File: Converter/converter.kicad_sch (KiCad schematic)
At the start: 39 parts, among them IC1 NCP5109ADR2G, IC2 NCP5109ADR2G, J3 XT30, J4 XT30

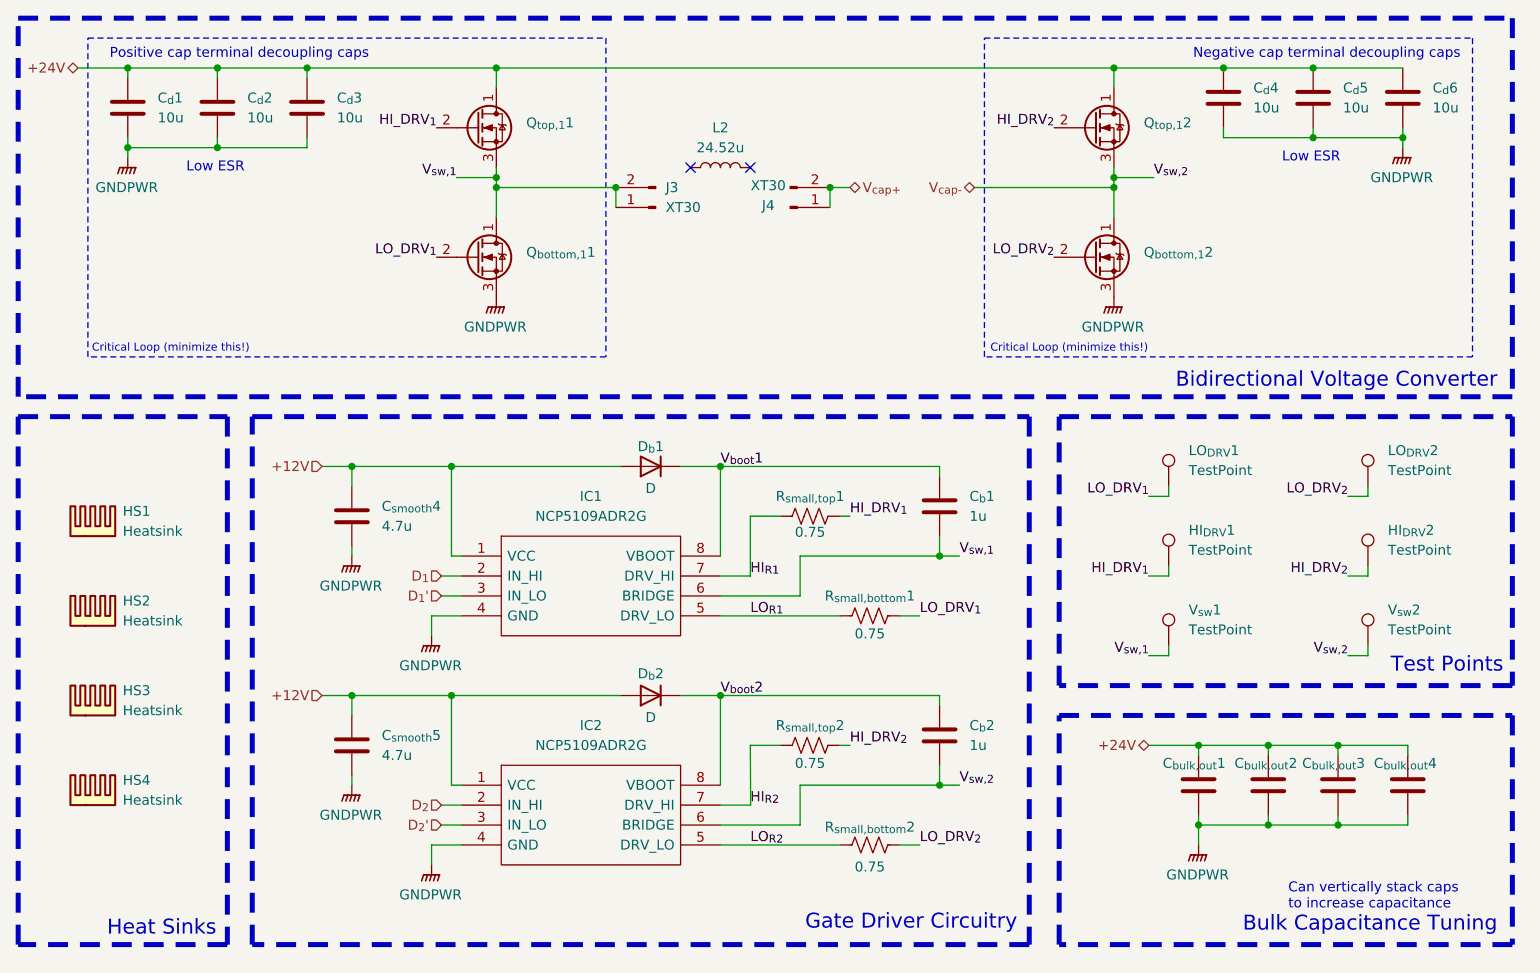
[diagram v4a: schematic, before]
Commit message: cleaned up PCB after meeting with BBJ
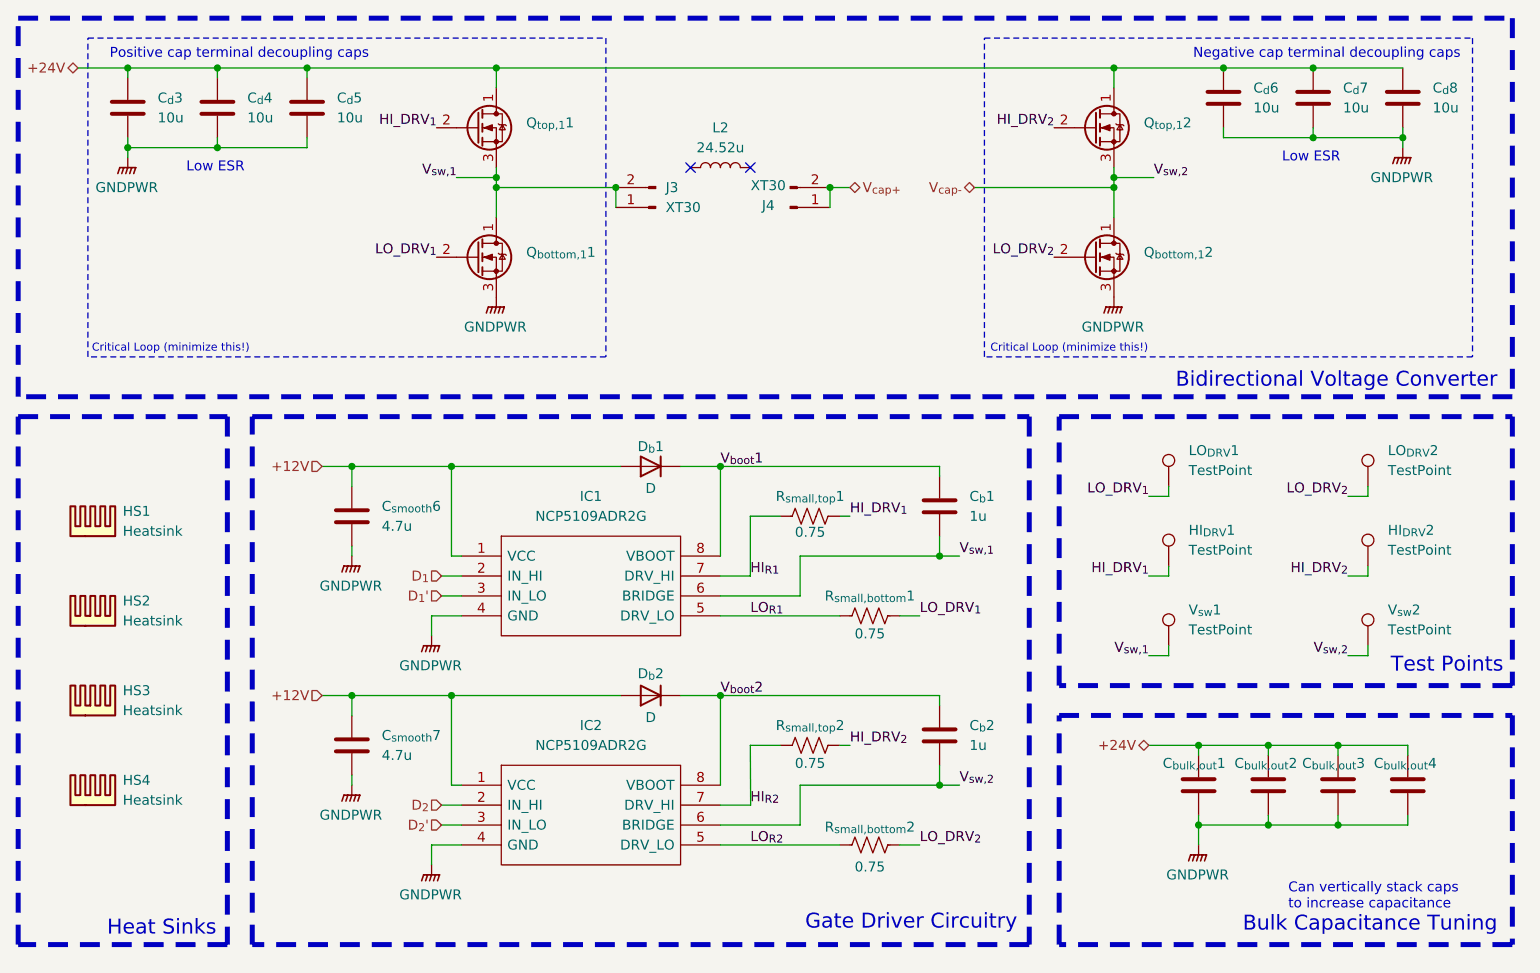
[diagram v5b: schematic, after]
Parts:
- renumbered C_{d}1 to C_{d}3, C_{d}2 to C_{d}4, C_{d}3 to C_{d}5, C_{d}4 to C_{d}6, C_{d}5 to C_{d}7, C_{d}6 to C_{d}8, C_{smooth}4 to C_{smooth}6, C_{smooth}5 to C_{smooth}7
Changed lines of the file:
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@@
 		(dnp no)
 		(fields_autoplaced yes)
-		(property "Reference" "#PWR025"
+		(property "Reference" "#PWR029"
 			(at 85.09 143.51 0)
 			(effects
@@
 			(project "Supercap"
 				(path "/98ee8313-37ab-4329-91ab-b5710476f82f/66de8ce3-68f9-4d35-858c-1420192a373c"
-					(reference "#PWR025")
+					(reference "#PWR029")
 					(unit 1)
 				)
@@
 		(dnp no)
 		(fields_autoplaced yes)
-		(property "Reference" "C_{smooth}5"
+		(property "Reference" "C_{smooth}7"
 			(at 88.9 132.0799 0)
 			(effects
@@
 			(project "Supercap"
 				(path "/98ee8313-37ab-4329-91ab-b5710476f82f/66de8ce3-68f9-4d35-858c-1420192a373c"
-					(reference "C_{smooth}5")
+					(reference "C_{smooth}7")
 					(unit 1)
 				)
@@
 		(on_board yes)
 		(dnp no)
-		(property "Reference" "C_{d}3"
+		(property "Reference" "C_{d}5"
 			(at 83.185 50.7999 0)
 			(effects
@@
 			(project "Supercap"
 				(path "/98ee8313-37ab-4329-91ab-b5710476f82f/66de8ce3-68f9-4d35-858c-1420192a373c"
-					(reference "C_{d}3")
+					(reference "C_{d}5")
 					(unit 1)
 				)
@@
 		(dnp no)
 		(fields_autoplaced yes)
-		(property "Reference" "#PWR023"
+		(property "Reference" "#PWR027"
 			(at 56.515 63.5 0)
 			(effects
@@
 			(project "Supercap"
 				(path "/98ee8313-37ab-4329-91ab-b5710476f82f/66de8ce3-68f9-4d35-858c-1420192a373c"
-					(reference "#PWR023")
+					(reference "#PWR027")
 					(unit 1)
 				)
@@
 		(dnp no)
 		(fields_autoplaced yes)
-		(property "Reference" "#PWR030"
+		(property "Reference" "#PWR034"
 			(at 193.04 151.13 0)
 			(effects
@@
 			(project "Supercap"
 				(path "/98ee8313-37ab-4329-91ab-b5710476f82f/66de8ce3-68f9-4d35-858c-1420192a373c"
-					(reference "#PWR030")
+					(reference "#PWR034")
 					(unit 1)
 				)
@@
 		(on_board yes)
 		(dnp no)
-		(property "Reference" "C_{d}4"
+		(property "Reference" "C_{d}6"
 			(at 200.025 49.5299 0)
 			(effects
@@
 			(project "Supercap"
 				(path "/98ee8313-37ab-4329-91ab-b5710476f82f/66de8ce3-68f9-4d35-858c-1420192a373c"
-					(reference "C_{d}4")
+					(reference "C_{d}6")
 					(unit 1)
 				)
@@
 		(dnp no)
 		(fields_autoplaced yes)
-		(property "Reference" "#PWR031"
+		(property "Reference" "#PWR035"
 			(at 219.075 62.23 0)
 			(effects
@@
 			(project "Supercap"
 				(path "/98ee8313-37ab-4329-91ab-b5710476f82f/66de8ce3-68f9-4d35-858c-1420192a373c"
-					(reference "#PWR031")
+					(reference "#PWR035")
 					(unit 1)
 				)
@@
 		(dnp no)
 		(fields_autoplaced yes)
-		(property "Reference" "#PWR029"
+		(property "Reference" "#PWR033"
 			(at 182.245 81.28 0)
 			(effects
@@
 			(project "Supercap"
 				(path "/98ee8313-37ab-4329-91ab-b5710476f82f/66de8ce3-68f9-4d35-858c-1420192a373c"
-					(reference "#PWR029")
+					(reference "#PWR033")
 					(unit 1)
 				)
@@
 		(dnp no)
 		(fields_autoplaced yes)
-		(property "Reference" "#PWR027"
+		(property "Reference" "#PWR031"
 			(at 95.25 153.67 0)
 			(effects
@@
 			(project "Supercap"
 				(path "/98ee8313-37ab-4329-91ab-b5710476f82f/66de8ce3-68f9-4d35-858c-1420192a373c"
-					(reference "#PWR027")
+					(reference "#PWR031")
 					(unit 1)
 				)
@@
 		(dnp no)
 		(fields_autoplaced yes)
-		(property "Reference" "C_{smooth}4"
+		(property "Reference" "C_{smooth}6"
 			(at 88.9 102.8699 0)
 			(effects
@@
 			(project "Supercap"
 				(path "/98ee8313-37ab-4329-91ab-b5710476f82f/66de8ce3-68f9-4d35-858c-1420192a373c"
-					(reference "C_{smooth}4")
+					(reference "C_{smooth}6")
 					(unit 1)
 				)
@@
 		(on_board yes)
 		(dnp no)
-		(property "Reference" "C_{d}1"
+		(property "Reference" "C_{d}3"
 			(at 60.325 50.7999 0)
 			(effects
@@
 			(project "Supercap"
 				(path "/98ee8313-37ab-4329-91ab-b5710476f82f/66de8ce3-68f9-4d35-858c-1420192a373c"
-					(reference "C_{d}1")
+					(reference "C_{d}3")
 					(unit 1)
 				)
@@
 		(on_board yes)
 		(dnp no)
-		(property "Reference" "C_{d}2"
+		(property "Reference" "C_{d}4"
 			(at 71.755 50.7999 0)
 			(effects
@@
 			(project "Supercap"
 				(path "/98ee8313-37ab-4329-91ab-b5710476f82f/66de8ce3-68f9-4d35-858c-1420192a373c"
-					(reference "C_{d}2")
+					(reference "C_{d}4")
 					(unit 1)
 				)
@@
 		(on_board yes)
 		(dnp no)
-		(property "Reference" "C_{d}6"
+		(property "Reference" "C_{d}8"
 			(at 222.885 49.5299 0)
 			(effects
@@
 			(project "Supercap"
 				(path "/98ee8313-37ab-4329-91ab-b5710476f82f/66de8ce3-68f9-4d35-858c-1420192a373c"
-					(reference "C_{d}6")
+					(reference "C_{d}8")
 					(unit 1)
 				)
@@
 		(on_board yes)
 		(dnp no)
-		(property "Reference" "C_{d}5"
+		(property "Reference" "C_{d}7"
 			(at 211.455 49.5299 0)
 			(effects
@@
 			(project "Supercap"
 				(path "/98ee8313-37ab-4329-91ab-b5710476f82f/66de8ce3-68f9-4d35-858c-1420192a373c"
-					(reference "C_{d}5")
+					(reference "C_{d}7")
 					(unit 1)
 				)
@@
 		(dnp no)
 		(fields_autoplaced yes)
-		(property "Reference" "#PWR028"
+		(property "Reference" "#PWR032"
 			(at 103.505 81.28 0)
 			(effects
@@
 			(project ""
 				(path "/98ee8313-37ab-4329-91ab-b5710476f82f/66de8ce3-68f9-4d35-858c-1420192a373c"
-					(reference "#PWR028")
+					(reference "#PWR032")
 					(unit 1)
 				)
@@
 		(dnp no)
 		(fields_autoplaced yes)
-		(property "Reference" "#PWR026"
+		(property "Reference" "#PWR030"
 			(at 95.25 124.46 0)
 			(effects
@@
 			(project "Supercap"
 				(path "/98ee8313-37ab-4329-91ab-b5710476f82f/66de8ce3-68f9-4d35-858c-1420192a373c"
-					(reference "#PWR026")
+					(reference "#PWR030")
 					(unit 1)
 				)
@@
 		(dnp no)
 		(fields_autoplaced yes)
-		(property "Reference" "#PWR024"
+		(property "Reference" "#PWR028"
 			(at 85.09 114.3 0)
 			(effects
@@
 			(project "Supercap"
 				(path "/98ee8313-37ab-4329-91ab-b5710476f82f/66de8ce3-68f9-4d35-858c-1420192a373c"
-					(reference "#PWR024")
+					(reference "#PWR028")
 					(unit 1)
 				)

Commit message: plotted standalone board and updated KiCAD BOM (not spreadsheet BOM)
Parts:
- Q_{bottom,1}1, Q_{bottom,1}2, Q_{top,1}1, Q_{top,1}2: Manufacturer_Part_Number IQDH35N03LM5CGSC -> IQDH35N03LM5CGSCATMA1; Mouser Part Number 726-IQFH36N04NM6ATMA -> 726-IQDH35N03LM5CGSC
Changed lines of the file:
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@@
 			)
 		)
-		(property "Manufacturer_Part_Number" "IQDH35N03LM5CGSC"
+		(property "Manufacturer_Part_Number" "IQDH35N03LM5CGSCATMA1"
 			(at 100.965 71.12 0)
 			(effects
@@
 			)
 		)
-		(property "Mouser Part Number" "726-IQFH36N04NM6ATMA"
+		(property "Mouser Part Number" "726-IQDH35N03LM5CGSC"
 			(at 100.965 71.12 0)
 			(effects
@@
 			)
 		)
-		(property "Manufacturer_Part_Number" "IQDH35N03LM5CGSC"
+		(property "Manufacturer_Part_Number" "IQDH35N03LM5CGSCATMA1"
 			(at 100.965 54.61 0)
 			(effects
@@
 			)
 		)
-		(property "Mouser Part Number" "726-IQFH36N04NM6ATMA"
+		(property "Mouser Part Number" "726-IQDH35N03LM5CGSC"
 			(at 100.965 54.61 0)
 			(effects
@@
 			)
 		)
-		(property "Manufacturer_Part_Number" "IQDH35N03LM5CGSC"
+		(property "Manufacturer_Part_Number" "IQDH35N03LM5CGSCATMA1"
 			(at 179.705 54.61 0)
 			(effects
@@
 			)
 		)
-		(property "Mouser Part Number" "726-IQFH36N04NM6ATMA"
+		(property "Mouser Part Number" "726-IQDH35N03LM5CGSC"
 			(at 179.705 54.61 0)
 			(effects
@@
 			)
 		)
-		(property "Manufacturer_Part_Number" "IQDH35N03LM5CGSC"
+		(property "Manufacturer_Part_Number" "IQDH35N03LM5CGSCATMA1"
 			(at 179.705 71.12 0)
 			(effects
@@
 			)
 		)
-		(property "Mouser Part Number" "726-IQFH36N04NM6ATMA"
+		(property "Mouser Part Number" "726-IQDH35N03LM5CGSC"
 			(at 179.705 71.12 0)
 			(effects
